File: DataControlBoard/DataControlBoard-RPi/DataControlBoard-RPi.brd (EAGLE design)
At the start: 160 x 100 mm, 9 parts, among them J1 USB3150-30-130-AMANUFACTURABLE, J2 USB3150-30-130-AMANUFACTURABLE, J3 USB3150-30-130-AMANUFACTURABLE, J4 USB3150-30-130-AMANUFACTURABLE, J5 USB3150-30-130-AMANUFACTURABLE, J6 USB3150-30-130-AMANUFACTURABLE

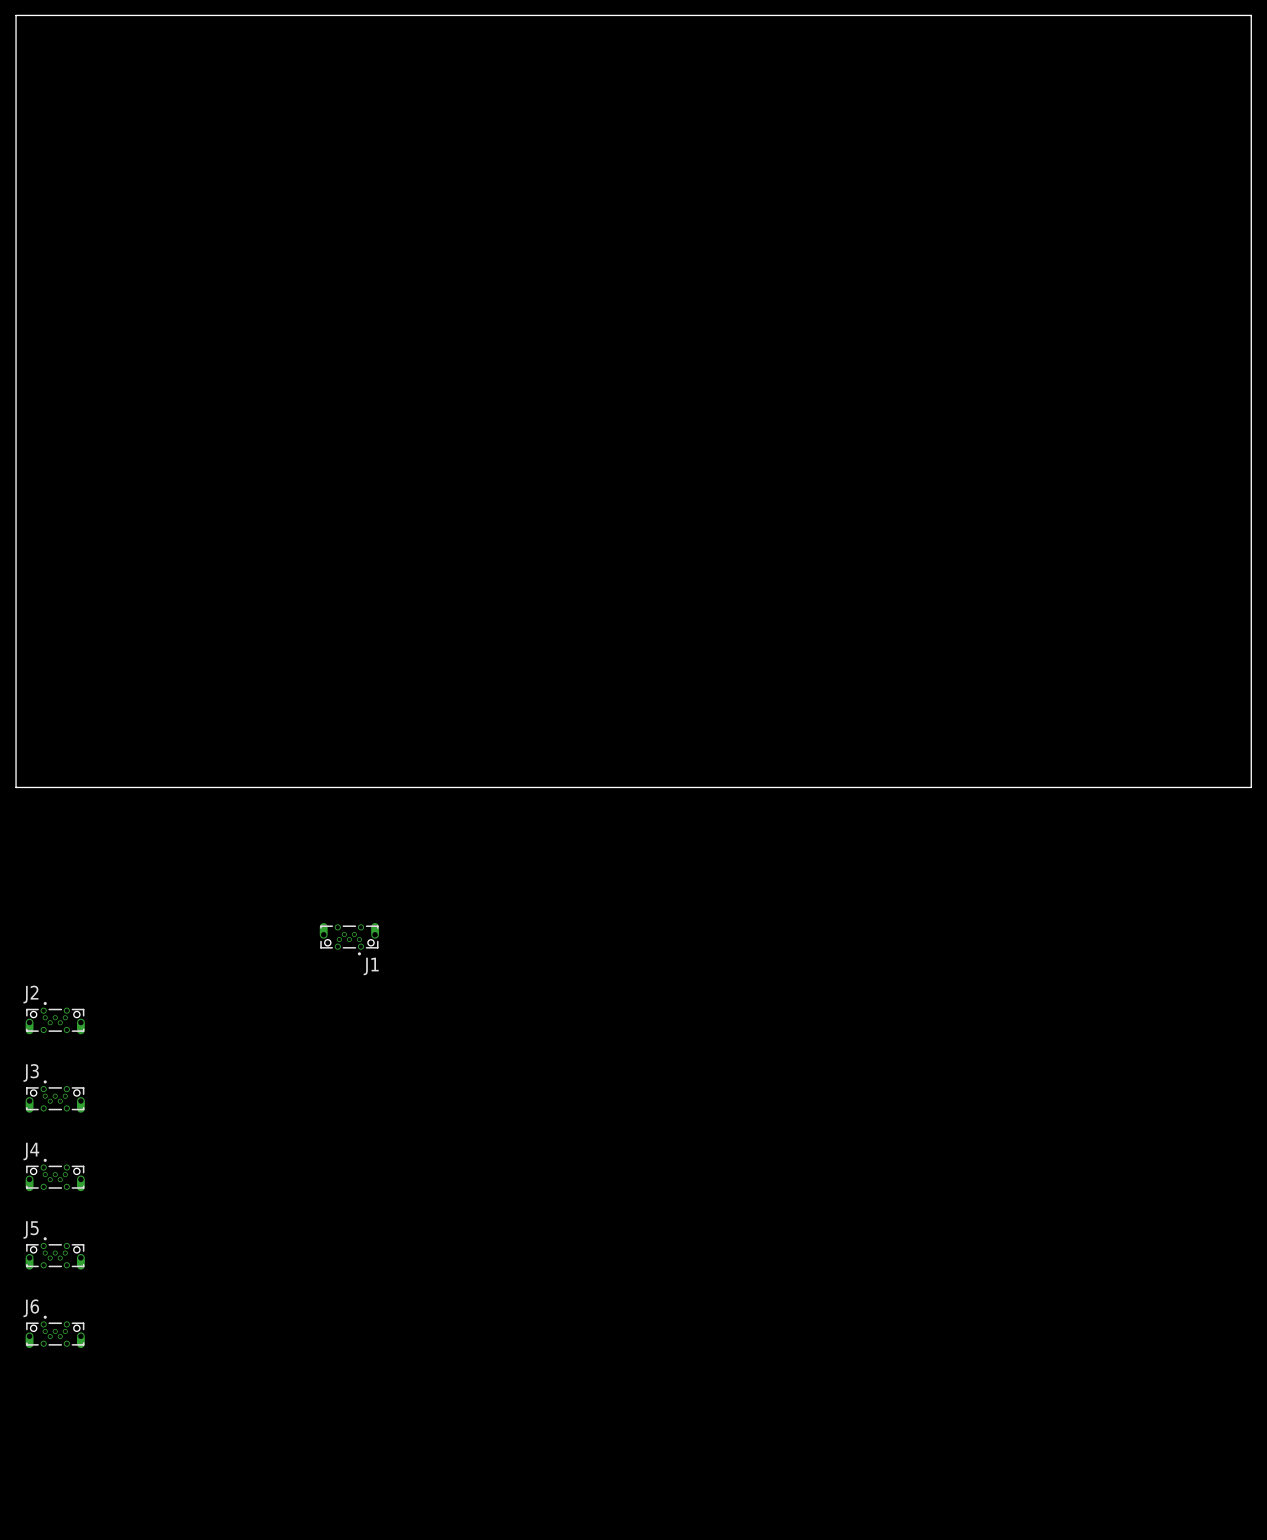
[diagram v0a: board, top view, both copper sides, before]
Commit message: Mechanical design of RPi Holder board nearly done. Power treaces routed
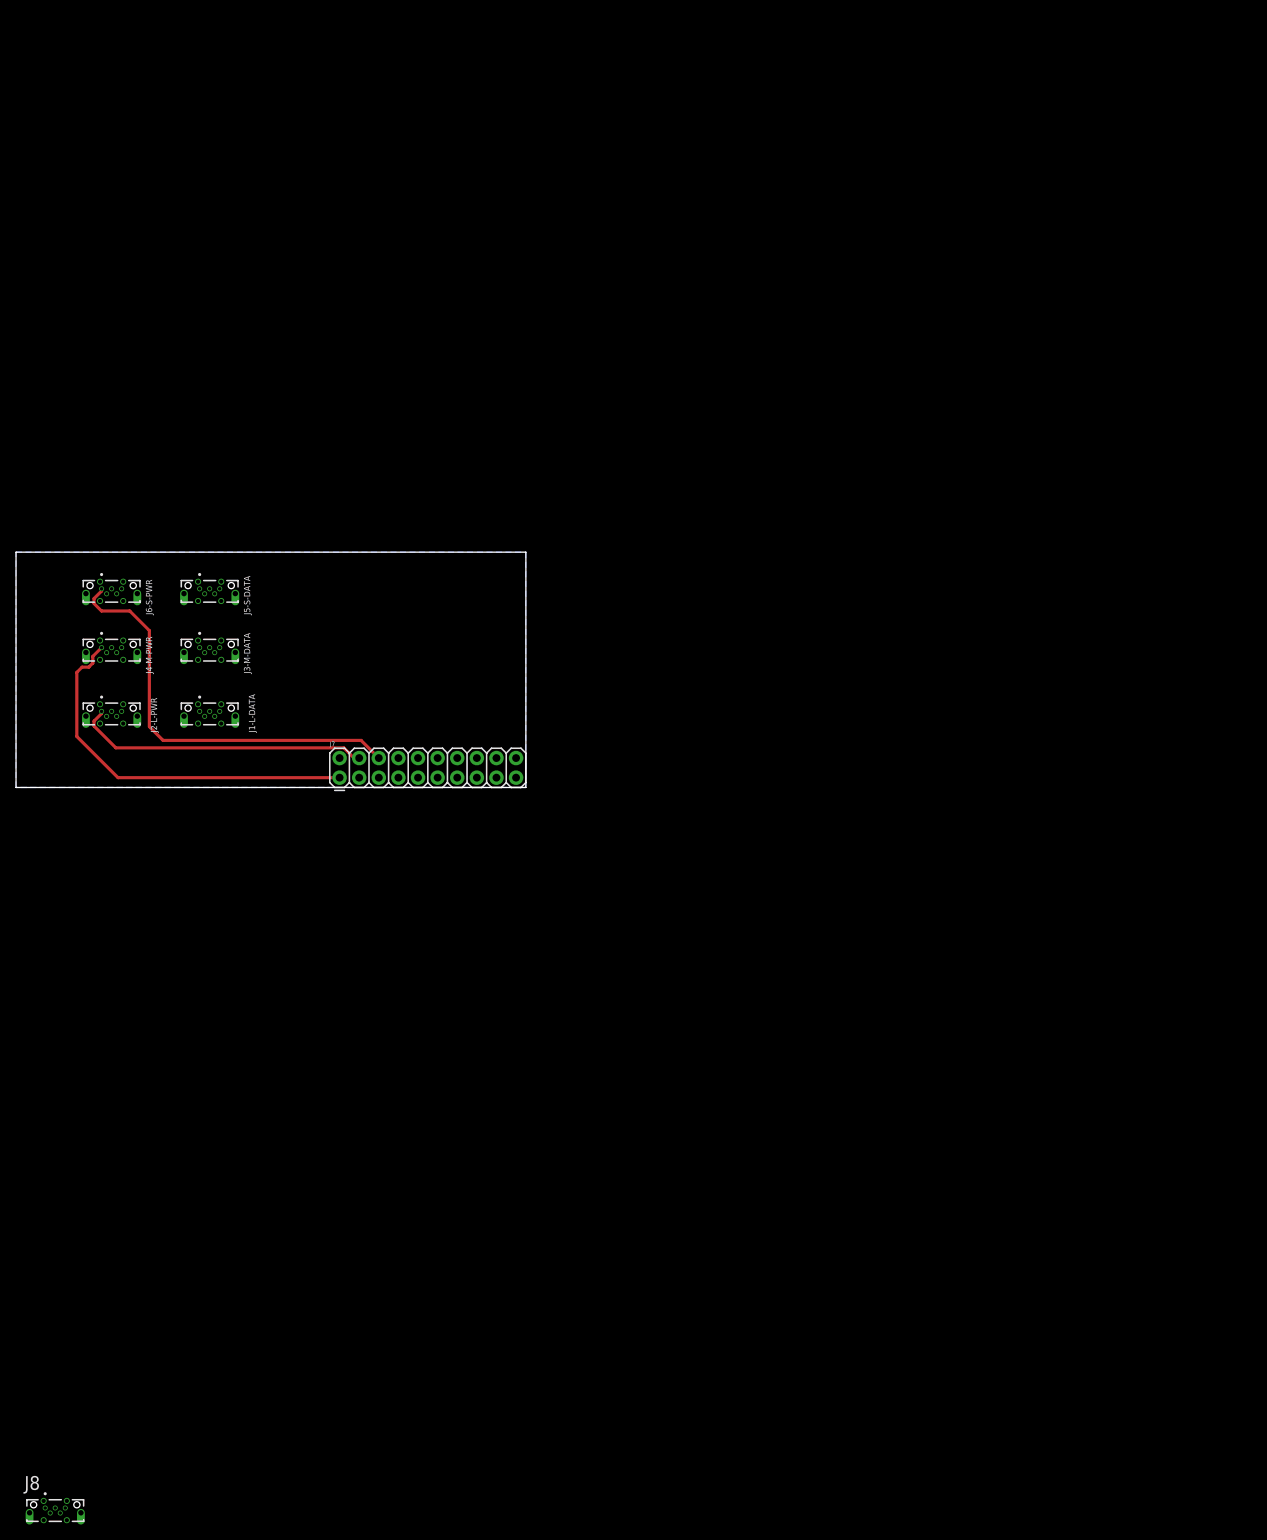
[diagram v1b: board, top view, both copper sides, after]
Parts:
- removed J1, J2, J3, J4, J5, J6: USB3150-30-130-AMANUFACTURABLE, RPi-Parts:GCT_USB3150-30-EASIER
- removed U$1, U$2, U$3: RPI-PLACEHOLDER, RPi-Parts:RPI-ZERO-EDGE
- added J1-L-DATA, J2-L-PWR, J3-M-DATA, J4-M-PWR, J5-S-DATA, J6-S-PWR, J8: USB3150-30-130-AMANUFACTURABLE, RPi-Parts:GCT_USB3150-30-EASIER
- added J7: (no value), SparkFun-Connectors:2X10
- added PH-L, PH-M, PH-S: RPI-PLACEHOLDER, RPi-Parts:RPI-ZERO-EDGE
- added U$4: LIDAR-CONV-PLACEHOLDER, RPi-Parts:LIDAR-PLACEHOLDER
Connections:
- new net 5V-DIG-CAM: J7.3
- new net 5V-DIG-LASER: J2-L-PWR.1, J7.4, J8.1
- new net 5V-DIG-MAG: J4-M-PWR.1, J7.1
- new net 5V-DIG-STA: J6-S-PWR.1, J7.6
- new net 5V-DIG-TX: J7.5
- new net GND: J1-L-DATA.5, J1-L-DATA.S1, J1-L-DATA.S2, J1-L-DATA.S3, J1-L-DATA.S4, J1-L-DATA.S5, J1-L-DATA.S6, J2-L-PWR.5, J2-L-PWR.S1, J2-L-PWR.S2, J2-L-PWR.S3, J2-L-PWR.S4, J2-L-PWR.S5, J2-L-PWR.S6, J3-M-DATA.5, J3-M-DATA.S1, J3-M-DATA.S2, J3-M-DATA.S3, J3-M-DATA.S4, J3-M-DATA.S5, J3-M-DATA.S6, J4-M-PWR.5, J4-M-PWR.S1, J4-M-PWR.S2, J4-M-PWR.S3, J4-M-PWR.S4, J4-M-PWR.S5, J4-M-PWR.S6, J5-S-DATA.5, J5-S-DATA.S1, J5-S-DATA.S2, J5-S-DATA.S3, J5-S-DATA.S4, J5-S-DATA.S5, J5-S-DATA.S6, J6-S-PWR.5, J6-S-PWR.S1, J6-S-PWR.S2, J6-S-PWR.S3, J6-S-PWR.S4, J6-S-PWR.S5, J6-S-PWR.S6, J7.2, J8.5, J8.S1, J8.S2, J8.S3, J8.S4, J8.S5, J8.S6
- new net LIDAR-D+: J8.3
- new net LIDAR-D-: J8.2
- new net N$14: J7.7
- new net N$15: J7.9
- new net N$16: J7.11
- new net N$17: J7.13
- new net N$18: J7.15
- new net N$19: J7.17
- new net N$20: J7.19
- new net N$3: J7.20
- new net N$4: J7.18
- new net N$5: J7.16
- new net N$6: J7.14
- new net N$7: J7.12
- new net N$8: J7.10
- new net N$9: J7.8
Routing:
- net 5V-DIG-STA: track 0.00 -> 54.8 mm
- net 5V-DIG-MAG: track 0.00 -> 49.6 mm
- net 5V-DIG-LASER: track 0.00 -> 38.4 mm
- added copper zone on layer 16, net GND
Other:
- board size 160 x 100 mm -> 66 x 30.5 mm
- board text added: "Laser RPi"
- board text added: "Magnet RPi"
- board text added: "Static RPi"

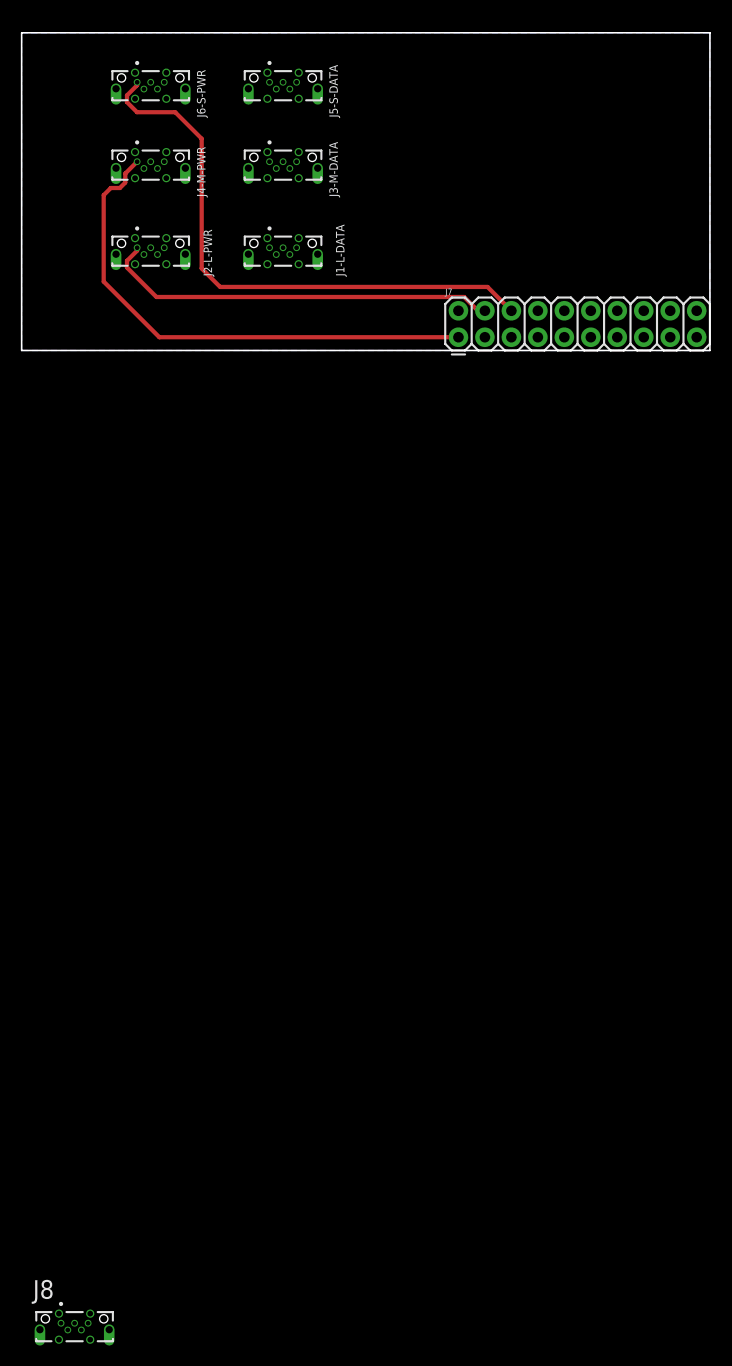
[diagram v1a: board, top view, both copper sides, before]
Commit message: Added USB to all RPi boards. Rearranged mechanical design slightly
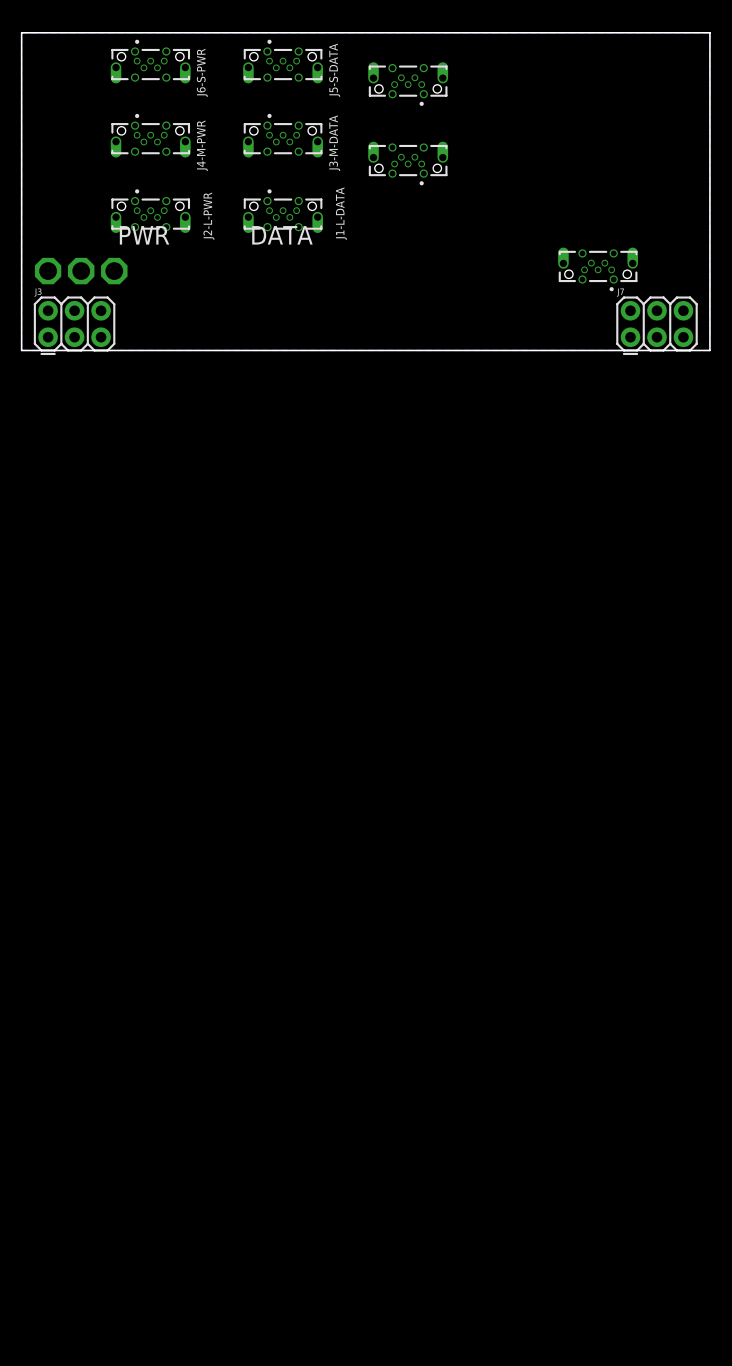
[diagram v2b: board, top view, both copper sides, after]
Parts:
- added J1, J2: USB3150-30-130-AMANUFACTURABLE, RPi-Parts:GCT_USB3150-30-EASIER
- added J3: (no value), SparkFun-Connectors:2X3
- added TP1, TP2, TP3: TPPAD1-17, testpad:P1-17
- J7: value (none) -> FEMALE 2x3; device SparkFun-Connectors:2X10 -> SparkFun-Connectors:2X3
- moved J8 114.0 mm to (55.3, 8.38), turned to 180 degrees
- moved U$4 107.2 mm to (55.4, 6.86)
- moved J7 16.5 mm to (58.4, 1.27)
- moved J1-L-DATA 3.56 mm to (25.1, 12.8)
- moved J2-L-PWR 3.56 mm to (12.4, 12.8)
- moved PH-L 3.56 mm to (65.7, 14.4)
- moved J3-M-DATA 2.54 mm to (25.1, 20.0)
- moved J4-M-PWR 2.54 mm to (12.4, 20.0)
- moved PH-M 2.54 mm to (65.7, 21.6)
- moved J5-S-DATA 2.03 mm to (25.1, 27.1)
- moved J6-S-PWR 2.03 mm to (12.4, 27.1)
- moved PH-S 2.03 mm to (65.7, 28.7)
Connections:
- removed net N$14: J7.7
- removed net N$15: J7.9
- removed net N$16: J7.11
- removed net N$17: J7.13
- removed net N$18: J7.15
- removed net N$19: J7.17
- removed net N$20: J7.19
- removed net N$5: J7.16
- removed net N$6: J7.14
- removed net N$7: J7.12
- removed net N$8: J7.10
- removed net N$9: J7.8
- new net MAG-D+: J1.3, J3-M-DATA.3
- new net MAG-D-: J1.2, J3-M-DATA.2
- new net N$2: J3.2, TP1.TP
- new net STA-D+: J2.3, J5-S-DATA.3
- new net STA-D-: J2.2, J5-S-DATA.2
- new net USB-5V-LID: J1-L-DATA.1, J8.1
- new net USB-5V-MAG: J1.1, J3-M-DATA.1
- new net USB-5V-STA: J2.1, J5-S-DATA.1
- net 5V-DIG-LASER: no longer J8.1
- net GND: now also J1.5, J1.S1, J1.S2, J1.S3, J1.S4, J1.S5, J1.S6, J2.5, J2.S1, J2.S2, J2.S3, J2.S4, J2.S5, J2.S6, J3.1, J3.3, J3.5
- net LIDAR-D+: now also J1-L-DATA.3
- net LIDAR-D-: now also J1-L-DATA.2
- net N$3: now also J3.4, TP2.TP; no longer J7.20
- net N$4: now also J3.6, TP3.TP; no longer J7.18
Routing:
- net 5V-DIG-STA: track 54.8 -> 0.00 mm
- net 5V-DIG-MAG: track 49.6 -> 0.00 mm
- net 5V-DIG-LASER: track 38.4 -> 0.00 mm
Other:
- board text added: "Boom Cam RPi"
- board text added: "DATA"
- board text added: "Magnet"
- board text added: "PWR"
- board text removed: "Laser RPi"
- board text removed: "Magnet RPi"

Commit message: Ready for Diff Pair routing
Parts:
- moved J1 20.9 mm to (55.4, 8.38)
- moved J8 18.5 mm to (37.0, 10.9)
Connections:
- net LIDAR-D+ renamed LIDAR-D_P
- net LIDAR-D- renamed LIDAR-D_N
- net MAG-D+ renamed MAG-D_P
- net MAG-D- renamed MAG-D_N
- net STA-D+ renamed STA-D_P
- net STA-D- renamed STA-D_N
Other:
- board text added: "Boom Cam"
- board text added: "Static"
- board text removed: "Boom Cam RPi"
- board text removed: "Static RPi"
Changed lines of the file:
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@@
 <wire x1="66.04" y1="30.48" x2="0" y2="30.48" width="0.1524" layer="20"/>
 <wire x1="0" y1="30.48" x2="0" y2="0" width="0.1524" layer="20"/>
-<text x="14.478" y="28.702" size="1.778" layer="51" font="vector">Static RPi</text>
+<text x="65.532" y="28.448" size="1.778" layer="51" font="vector" rot="R180">Static</text>
 <text x="65.786" y="21.336" size="1.778" layer="51" font="vector" rot="R180">Magnet</text>
-<text x="0" y="12.7" size="1.778" layer="51" font="vector">Boom Cam RPi</text>
+<text x="66.04" y="13.97" size="1.778" layer="51" font="vector" rot="R180">Boom Cam</text>
 <text x="21.9075" y="10.16" size="1.778" layer="21">DATA</text>
 <text x="9.2075" y="10.16" size="1.778" layer="21">PWR</text>
@@
 <classes>
 <class number="0" name="default" width="0" drill="0">
+</class>
+<class number="1" name="USB_diff" width="0.8128" drill="0">
+<clearance class="1" value="0.2032"/>
 </class>
 </classes>
@@
 </element>
 <element name="U$4" library="RPi-Parts" package="LIDAR-PLACEHOLDER" value="LIDAR-CONV-PLACEHOLDER" x="55.372" y="6.858" smashed="yes"/>
-<element name="J8" library="RPi-Parts" package="GCT_USB3150-30-EASIER" value="USB3150-30-130-AMANUFACTURABLE" x="55.3085" y="8.382" smashed="yes" rot="R180"/>
-<element name="J1" library="RPi-Parts" package="GCT_USB3150-30-EASIER" value="USB3150-30-130-AMANUFACTURABLE" x="37.084" y="18.542" smashed="yes" rot="R180"/>
+<element name="J8" library="RPi-Parts" package="GCT_USB3150-30-EASIER" value="USB3150-30-130-AMANUFACTURABLE" x="37.0205" y="10.922" smashed="yes" rot="R180"/>
+<element name="J1" library="RPi-Parts" package="GCT_USB3150-30-EASIER" value="USB3150-30-130-AMANUFACTURABLE" x="55.372" y="8.382" smashed="yes" rot="R180"/>
 <element name="J2" library="RPi-Parts" package="GCT_USB3150-30-EASIER" value="USB3150-30-130-AMANUFACTURABLE" x="37.084" y="26.162" smashed="yes" rot="R180"/>
 <element name="J3" library="SparkFun-Connectors" library_urn="urn:adsk.eagle:library:513" package="2X3" package3d_urn="urn:adsk.eagle:package:38016/1" value="" x="2.54" y="1.27" smashed="yes">
@@
 <contactref element="J7" pad="5"/>
 </signal>
-<signal name="LIDAR-D-">
-<contactref element="J8" pad="2"/>
-<contactref element="J1-L-DATA" pad="2"/>
-<wire x1="24.4325" y1="12.7635" x2="55.9585" y2="8.382" width="0" layer="19" extent="1-1"/>
-</signal>
-<signal name="LIDAR-D+">
+<signal name="LIDAR-D_P">
 <contactref element="J8" pad="3"/>
 <contactref element="J1-L-DATA" pad="3"/>
-<wire x1="25.0825" y1="13.4135" x2="55.3085" y2="7.732" width="0" layer="19" extent="1-1"/>
-</signal>
-<signal name="MAG-D+">
+<wire x1="25.0825" y1="13.4135" x2="37.0205" y2="10.272" width="0" layer="19" extent="1-1"/>
+</signal>
+<signal name="MAG-D_P">
 <contactref element="J1" pad="3"/>
 <contactref element="J3-M-DATA" pad="3"/>
-<wire x1="25.0825" y1="20.6525" x2="37.084" y2="17.892" width="0" layer="19" extent="1-1"/>
-</signal>
-<signal name="MAG-D-">
-<contactref element="J1" pad="2"/>
-<contactref element="J3-M-DATA" pad="2"/>
-<wire x1="24.4325" y1="20.0025" x2="37.734" y2="18.542" width="0" layer="19" extent="1-1"/>
+<wire x1="25.0825" y1="20.6525" x2="55.372" y2="7.732" width="0" layer="19" extent="1-1"/>
 </signal>
 <signal name="USB-5V-MAG">
 <contactref element="J1" pad="1"/>
 <contactref element="J3-M-DATA" pad="1"/>
-<wire x1="23.7825" y1="20.6525" x2="38.384" y2="17.892" width="0" layer="19" extent="1-1"/>
-</signal>
-<signal name="STA-D+">
-<contactref element="J2" pad="3"/>
-<contactref element="J5-S-DATA" pad="3"/>
-<wire x1="25.0825" y1="27.7645" x2="37.084" y2="25.512" width="0" layer="19" extent="1-1"/>
-</signal>
-<signal name="STA-D-">
+<wire x1="23.7825" y1="20.6525" x2="56.672" y2="7.732" width="0" layer="19" extent="1-1"/>
+</signal>
+<signal name="STA-D_N">
 <contactref element="J2" pad="2"/>
 <contactref element="J5-S-DATA" pad="2"/>
@@
 <contactref element="J8" pad="1"/>
 <contactref element="J1-L-DATA" pad="1"/>
-<wire x1="23.7825" y1="13.4135" x2="56.6085" y2="7.732" width="0" layer="19" extent="1-1"/>
+<wire x1="23.7825" y1="13.4135" x2="38.3205" y2="10.272" width="0" layer="19" extent="1-1"/>
 </signal>
 <signal name="N$2">
@@
 <wire x1="7.62" y1="3.81" x2="8.89" y2="7.62" width="0" layer="19" extent="1-1"/>
 </signal>
+<signal name="MAG-D_N">
+<contactref element="J3-M-DATA" pad="2"/>
+<contactref element="J1" pad="2"/>
+<wire x1="24.4325" y1="20.0025" x2="56.022" y2="8.382" width="0" layer="19" extent="1-1"/>
+</signal>
+<signal name="STA-D_P">
+<contactref element="J2" pad="3"/>
+<contactref element="J5-S-DATA" pad="3"/>
+<wire x1="25.0825" y1="27.7645" x2="37.084" y2="25.512" width="0" layer="19" extent="1-1"/>
+</signal>
+<signal name="LIDAR-D_N">
+<contactref element="J1-L-DATA" pad="2"/>
+<contactref element="J8" pad="2"/>
+<wire x1="24.4325" y1="12.7635" x2="37.6705" y2="10.922" width="0" layer="19" extent="1-1"/>
+</signal>
 </signals>
